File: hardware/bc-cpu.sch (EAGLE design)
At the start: 84 parts, among them J1 BATTERIES, J2 PHT, J3 LED Matrix, J5 BRK5, U1 R-735.0P, U2 MAX11632EEG+, U3 MAX11632EEG+, U4 AD1584BRTZ

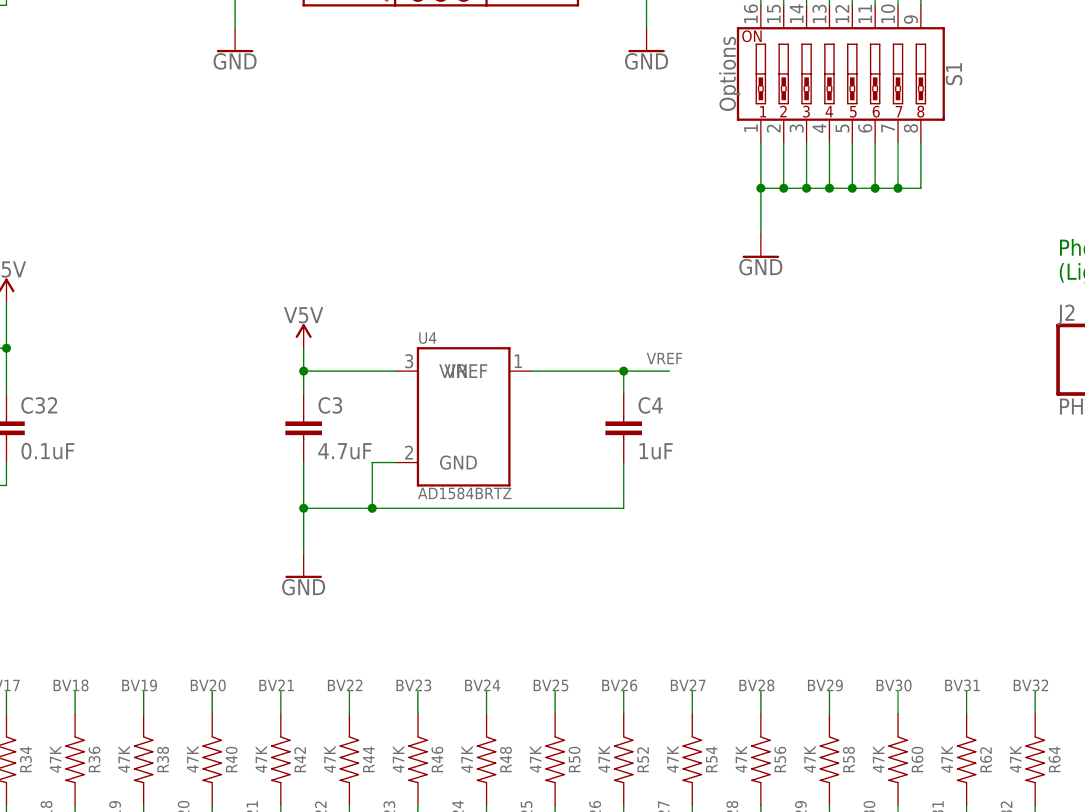
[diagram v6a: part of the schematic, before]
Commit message: All routed, DRC checks passing
Also removed drill holes from Arduino Nano lib -- they were translating
into the board for no reason. Replaced them with just silkscreen.
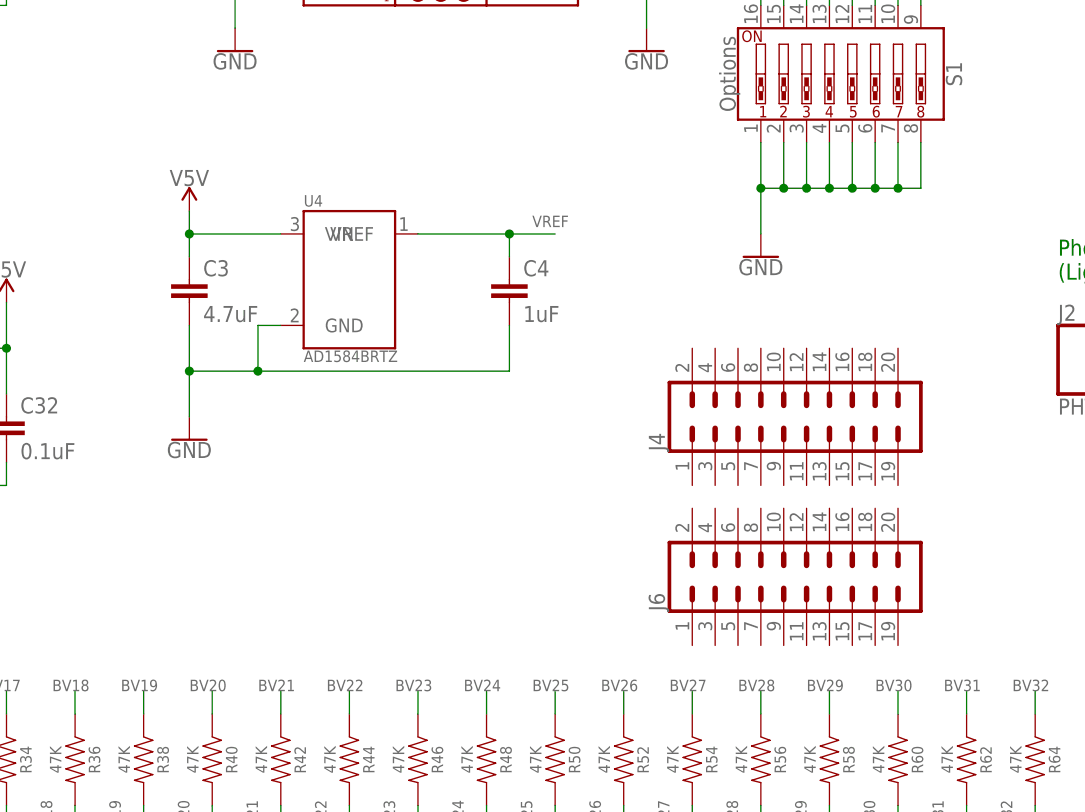
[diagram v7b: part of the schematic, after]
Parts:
- added J4, J6: (no value), SparkFun-Connectors:CONN_10X2NOSILK
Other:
- moved on the sheet: C3, C4, U4
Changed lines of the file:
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@@
 <part name="POWER" library="SparkFun-Connectors" deviceset="CONN_02" device="" value="12V"/>
 <part name="J5" library="SparkFun-Connectors" deviceset="CONN_02" device="" value="BRK5"/>
+<part name="J4" library="SparkFun-Connectors" deviceset="CONN_10X2" device="NOSILK"/>
+<part name="J6" library="SparkFun-Connectors" deviceset="CONN_10X2" device="NOSILK"/>
 </parts>
 <sheets>
@@
 <instance part="R63" gate="G$1" x="243.84" y="33.02" rot="R270"/>
 <instance part="R64" gate="G$1" x="243.84" y="48.26" rot="R270"/>
-<instance part="U4" gate="U1" x="180.34" y="86.36"/>
-<instance part="C3" gate="G$1" x="162.56" y="86.36"/>
-<instance part="C4" gate="G$1" x="198.12" y="86.36"/>
-<instance part="V5V1" gate="G$2" x="162.56" y="93.98"/>
-<instance part="GND3" gate="1" x="162.56" y="68.58"/>
+<instance part="U4" gate="U1" x="167.64" y="101.6"/>
+<instance part="C3" gate="G$1" x="149.86" y="101.6"/>
+<instance part="C4" gate="G$1" x="185.42" y="101.6"/>
+<instance part="V5V1" gate="G$2" x="149.86" y="109.22"/>
+<instance part="GND3" gate="1" x="149.86" y="83.82"/>
 <instance part="V5V2" gate="G$2" x="129.54" y="99.06"/>
 <instance part="V5V3" gate="G$2" x="129.54" y="152.4"/>
@@
 <instance part="POWER" gate="G$1" x="7.62" y="157.48"/>
 <instance part="J5" gate="G$1" x="50.8" y="162.56"/>
+<instance part="J4" gate="G$1" x="215.9" y="86.36" rot="R90"/>
+<instance part="J6" gate="G$1" x="215.9" y="68.58" rot="R90"/>
 </instances>
 <busses>
@@
 <segment>
 <pinref part="C3" gate="G$1" pin="2"/>
-<wire x1="162.56" y1="81.28" x2="162.56" y2="76.2" width="0.1524" layer="91"/>
+<wire x1="149.86" y1="96.52" x2="149.86" y2="91.44" width="0.1524" layer="91"/>
 <pinref part="GND3" gate="1" pin="GND"/>
 <pinref part="C4" gate="G$1" pin="2"/>
-<wire x1="162.56" y1="76.2" x2="162.56" y2="71.12" width="0.1524" layer="91"/>
-<wire x1="198.12" y1="81.28" x2="198.12" y2="76.2" width="0.1524" layer="91"/>
-<wire x1="198.12" y1="76.2" x2="170.18" y2="76.2" width="0.1524" layer="91"/>
-<junction x="162.56" y="76.2"/>
+<wire x1="149.86" y1="91.44" x2="149.86" y2="86.36" width="0.1524" layer="91"/>
+<wire x1="185.42" y1="96.52" x2="185.42" y2="91.44" width="0.1524" layer="91"/>
+<wire x1="185.42" y1="91.44" x2="157.48" y2="91.44" width="0.1524" layer="91"/>
+<junction x="149.86" y="91.44"/>
 <pinref part="U4" gate="U1" pin="GND"/>
-<wire x1="170.18" y1="76.2" x2="162.56" y2="76.2" width="0.1524" layer="91"/>
-<wire x1="172.72" y1="81.28" x2="170.18" y2="81.28" width="0.1524" layer="91"/>
-<wire x1="170.18" y1="81.28" x2="170.18" y2="76.2" width="0.1524" layer="91"/>
-<junction x="170.18" y="76.2"/>
+<wire x1="157.48" y1="91.44" x2="149.86" y2="91.44" width="0.1524" layer="91"/>
+<wire x1="160.02" y1="96.52" x2="157.48" y2="96.52" width="0.1524" layer="91"/>
+<wire x1="157.48" y1="96.52" x2="157.48" y2="91.44" width="0.1524" layer="91"/>
+<junction x="157.48" y="91.44"/>
 </segment>
 <segment>
@@
 <segment>
 <pinref part="U4" gate="U1" pin="VIN"/>
-<wire x1="172.72" y1="91.44" x2="162.56" y2="91.44" width="0.1524" layer="91"/>
+<wire x1="160.02" y1="106.68" x2="149.86" y2="106.68" width="0.1524" layer="91"/>
 <pinref part="C3" gate="G$1" pin="1"/>
-<wire x1="162.56" y1="91.44" x2="162.56" y2="88.9" width="0.1524" layer="91"/>
+<wire x1="149.86" y1="106.68" x2="149.86" y2="104.14" width="0.1524" layer="91"/>
 <pinref part="V5V1" gate="G$2" pin="VCC_1"/>
-<wire x1="162.56" y1="91.44" x2="162.56" y2="93.98" width="0.1524" layer="91"/>
-<junction x="162.56" y="91.44"/>
+<wire x1="149.86" y1="106.68" x2="149.86" y2="109.22" width="0.1524" layer="91"/>
+<junction x="149.86" y="106.68"/>
 </segment>
 <segment>
@@
 <segment>
 <pinref part="U4" gate="U1" pin="VREF"/>
-<wire x1="187.96" y1="91.44" x2="198.12" y2="91.44" width="0.1524" layer="91"/>
+<wire x1="175.26" y1="106.68" x2="185.42" y2="106.68" width="0.1524" layer="91"/>
 <pinref part="C4" gate="G$1" pin="1"/>
-<wire x1="198.12" y1="91.44" x2="198.12" y2="88.9" width="0.1524" layer="91"/>
-<wire x1="198.12" y1="91.44" x2="203.2" y2="91.44" width="0.1524" layer="91"/>
-<junction x="198.12" y="91.44"/>
-<label x="200.66" y="92.202" size="1.27" layer="95"/>
-</segment>
-<segment>
+<wire x1="185.42" y1="106.68" x2="185.42" y2="104.14" width="0.1524" layer="91"/>
+<wire x1="185.42" y1="106.68" x2="190.5" y2="106.68" width="0.1524" layer="91"/>
+<junction x="185.42" y="106.68"/>
+<label x="187.96" y="107.442" size="1.27" layer="95"/>
+</segment>
+<segment>

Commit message: Text, labels, positioning
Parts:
- J2: value PHT -> PHOTO
- J3: value LED Matrix -> LED MATRIX
- R65: value (none) -> 10K
- S1: value Options -> OPTIONS
- renumbered ARDUINO_NANO to ARDUINO
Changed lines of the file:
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@@
 <part name="U3" library="MAX-11632" deviceset="MAX-11632" device="QSOP24" value="MAX11632EEG+"/>
 <part name="J1" library="SparkFun-Connectors" deviceset="CONN_20X2" device="SHROUDED" value="BATTERIES"/>
-<part name="ARDUINO_NANO" library="ArduinoNanoV30" deviceset="ARDUINO_NANO" device=""/>
+<part name="ARDUINO" library="ArduinoNanoV30" deviceset="ARDUINO_NANO" device=""/>
 <part name="R1" library="SparkFun-Resistors" deviceset="RESISTOR" device="1206" value="1.5K"/>
 <part name="R2" library="SparkFun-Resistors" deviceset="RESISTOR" device="1206" value="47K"/>
@@
 <part name="GND8" library="SparkFun-PowerSymbols" deviceset="GND" device=""/>
 <part name="V5V4" library="SparkFun-PowerSymbols" deviceset="VCC_1" device="" value="V5V"/>
-<part name="J3" library="SparkFun-Connectors" deviceset="CONN_05X2" device="SHD" value="LED Matrix"/>
-<part name="S1" library="SparkFun-Switches" deviceset="DIP-08" device="-PTH" value="Options"/>
+<part name="J3" library="SparkFun-Connectors" deviceset="CONN_05X2" device="SHD" value="LED MATRIX"/>
+<part name="S1" library="SparkFun-Switches" deviceset="DIP-08" device="-PTH" value="OPTIONS"/>
 <part name="GND9" library="SparkFun-PowerSymbols" deviceset="GND" device=""/>
-<part name="R65" library="SparkFun-Resistors" deviceset="RESISTOR" device="AXIAL-0.3" value=" "/>
+<part name="R65" library="SparkFun-Resistors" deviceset="RESISTOR" device="AXIAL-0.3" value="10K"/>
 <part name="GND10" library="SparkFun-PowerSymbols" deviceset="GND" device=""/>
-<part name="J2" library="SparkFun-Connectors" deviceset="CONN_02" device="" value="PHT"/>
+<part name="J2" library="SparkFun-Connectors" deviceset="CONN_02" device="" value="PHOTO"/>
 <part name="POWER" library="SparkFun-Connectors" deviceset="CONN_02" device="" value="12V"/>
 <part name="J5" library="SparkFun-Connectors" deviceset="CONN_02" device="" value="BRK5"/>
@@
 <instance part="U3" gate="U1" x="96.52" y="99.06"/>
 <instance part="J1" gate="G$1" x="20.32" y="93.98"/>
-<instance part="ARDUINO_NANO" gate="G$1" x="177.8" y="157.48" rot="R180"/>
+<instance part="ARDUINO" gate="G$1" x="177.8" y="157.48" rot="R180"/>
 <instance part="R1" gate="G$1" x="7.62" y="33.02" rot="R270"/>
 <instance part="R2" gate="G$1" x="7.62" y="48.26" rot="R270"/>
@@
 </segment>
 <segment>
-<pinref part="ARDUINO_NANO" gate="G$1" pin="GND@2"/>
+<pinref part="ARDUINO" gate="G$1" pin="GND@2"/>
 <wire x1="157.48" y1="137.16" x2="154.94" y2="137.16" width="0.1524" layer="91"/>
 <pinref part="GND6" gate="1" pin="GND"/>
@@
 </segment>
 <segment>
-<pinref part="ARDUINO_NANO" gate="G$1" pin="GND@1"/>
+<pinref part="ARDUINO" gate="G$1" pin="GND@1"/>
 <wire x1="198.12" y1="142.24" x2="200.66" y2="142.24" width="0.1524" layer="91"/>
 <pinref part="GND4" gate="1" pin="GND"/>
@@
 </segment>
 <segment>
-<pinref part="ARDUINO_NANO" gate="G$1" pin="5V"/>
+<pinref part="ARDUINO" gate="G$1" pin="5V"/>
 <wire x1="157.48" y1="142.24" x2="144.78" y2="142.24" width="0.1524" layer="91"/>
 <pinref part="V5V4" gate="G$2" pin="VCC_1"/>
@@
 </segment>
 <segment>
-<pinref part="ARDUINO_NANO" gate="G$1" pin="SCK/D13"/>
+<pinref part="ARDUINO" gate="G$1" pin="SCK/D13"/>
 <wire x1="157.48" y1="170.18" x2="149.86" y2="170.18" width="0.1524" layer="91"/>
 <label x="149.86" y="170.18" size="1.778" layer="95"/>
@@
 </segment>
 <segment>
-<pinref part="ARDUINO_NANO" gate="G$1" pin="D11/MOSI"/>
+<pinref part="ARDUINO" gate="G$1" pin="D11/MOSI"/>
 <wire x1="198.12" y1="167.64" x2="205.74" y2="167.64" width="0.1524" layer="91"/>
 <label x="203.2" y="167.64" size="1.778" layer="95"/>
@@
 </segment>
 <segment>
-<pinref part="ARDUINO_NANO" gate="G$1" pin="D12/MISO"/>
+<pinref part="ARDUINO" gate="G$1" pin="D12/MISO"/>
 <wire x1="198.12" y1="170.18" x2="205.74" y2="170.18" width="0.1524" layer="91"/>
 <label x="203.2" y="170.18" size="1.778" layer="95"/>
@@
 </segment>
 <segment>
-<pinref part="ARDUINO_NANO" gate="G$1" pin="D10/OC1B/!SS"/>
+<pinref part="ARDUINO" gate="G$1" pin="D10/OC1B/!SS"/>
 <wire x1="198.12" y1="165.1" x2="205.74" y2="165.1" width="0.1524" layer="91"/>
 <label x="203.2" y="165.1" size="1.778" layer="95"/>
@@
 </segment>
 <segment>
-<pinref part="ARDUINO_NANO" gate="G$1" pin="D9/OC1A"/>
+<pinref part="ARDUINO" gate="G$1" pin="D9/OC1A"/>
 <wire x1="198.12" y1="162.56" x2="205.74" y2="162.56" width="0.1524" layer="91"/>
 <label x="203.2" y="162.56" size="1.778" layer="95"/>
@@
 </segment>
 <segment>
-<pinref part="ARDUINO_NANO" gate="G$1" pin="ADC5/SCL/A5"/>
+<pinref part="ARDUINO" gate="G$1" pin="ADC5/SCL/A5"/>
 <wire x1="157.48" y1="149.86" x2="149.86" y2="149.86" width="0.1524" layer="91"/>
 <label x="149.86" y="149.86" size="1.778" layer="95"/>
@@
 </segment>
 <segment>
-<pinref part="ARDUINO_NANO" gate="G$1" pin="ADC4/SDA/A4"/>
+<pinref part="ARDUINO" gate="G$1" pin="ADC4/SDA/A4"/>
 <wire x1="157.48" y1="152.4" x2="149.86" y2="152.4" width="0.1524" layer="91"/>
 <label x="149.86" y="152.4" size="1.778" layer="95"/>
@@
 <net name="DIP1" class="0">
 <segment>
-<pinref part="ARDUINO_NANO" gate="G$1" pin="D2/INT0"/>
+<pinref part="ARDUINO" gate="G$1" pin="D2/INT0"/>
 <wire x1="198.12" y1="144.78" x2="205.74" y2="144.78" width="0.1524" layer="91"/>
 <wire x1="205.74" y1="144.78" x2="213.36" y2="137.16" width="0.1524" layer="91"/>
@@
 <net name="DIP2" class="0">
 <segment>
-<pinref part="ARDUINO_NANO" gate="G$1" pin="D3/INT1"/>
+<pinref part="ARDUINO" gate="G$1" pin="D3/INT1"/>
 <wire x1="198.12" y1="147.32" x2="205.74" y2="147.32" width="0.1524" layer="91"/>
 <wire x1="205.74" y1="147.32" x2="215.9" y2="137.16" width="0.1524" layer="91"/>
@@
 <net name="DIP3" class="0">
 <segment>
-<pinref part="ARDUINO_NANO" gate="G$1" pin="D4/T0"/>
+<pinref part="ARDUINO" gate="G$1" pin="D4/T0"/>
 <wire x1="198.12" y1="149.86" x2="205.74" y2="149.86" width="0.1524" layer="91"/>
 <wire x1="205.74" y1="149.86" x2="218.44" y2="137.16" width="0.1524" layer="91"/>
@@
 <net name="DIP4" class="0">
 <segment>
-<pinref part="ARDUINO_NANO" gate="G$1" pin="D5/T1"/>
+<pinref part="ARDUINO" gate="G$1" pin="D5/T1"/>
 <wire x1="198.12" y1="152.4" x2="205.74" y2="152.4" width="0.1524" layer="91"/>
 <wire x1="205.74" y1="152.4" x2="220.98" y2="137.16" width="0.1524" layer="91"/>
@@
 <net name="DIP5" class="0">
 <segment>
-<pinref part="ARDUINO_NANO" gate="G$1" pin="D6/AIN0"/>
+<pinref part="ARDUINO" gate="G$1" pin="D6/AIN0"/>
 <wire x1="198.12" y1="154.94" x2="205.74" y2="154.94" width="0.1524" layer="91"/>
 <wire x1="205.74" y1="154.94" x2="223.52" y2="137.16" width="0.1524" layer="91"/>
@@
 <net name="DIP6" class="0">
 <segment>
-<pinref part="ARDUINO_NANO" gate="G$1" pin="D7/AIN1"/>
+<pinref part="ARDUINO" gate="G$1" pin="D7/AIN1"/>
 <wire x1="198.12" y1="157.48" x2="205.74" y2="157.48" width="0.1524" layer="91"/>
 <wire x1="205.74" y1="157.48" x2="226.06" y2="137.16" width="0.1524" layer="91"/>
@@
 <net name="DIP7" class="0">
 <segment>
-<pinref part="ARDUINO_NANO" gate="G$1" pin="D8/CLK0"/>
+<pinref part="ARDUINO" gate="G$1" pin="D8/CLK0"/>
 <wire x1="198.12" y1="160.02" x2="205.74" y2="160.02" width="0.1524" layer="91"/>
 <wire x1="205.74" y1="160.02" x2="228.6" y2="137.16" width="0.1524" layer="91"/>
@@
 </segment>
 <segment>
-<pinref part="ARDUINO_NANO" gate="G$1" pin="ADC0/A0"/>
+<pinref part="ARDUINO" gate="G$1" pin="ADC0/A0"/>
 <wire x1="157.48" y1="162.56" x2="149.86" y2="162.56" width="0.1524" layer="91"/>
 <label x="149.86" y="162.56" size="1.778" layer="95"/>
@@
 </segment>
 <segment>
-<pinref part="ARDUINO_NANO" gate="G$1" pin="ADC1/A1"/>
+<pinref part="ARDUINO" gate="G$1" pin="ADC1/A1"/>
 <wire x1="157.48" y1="160.02" x2="149.86" y2="160.02" width="0.1524" layer="91"/>
 <label x="149.86" y="160.02" size="1.778" layer="95"/>
@@
 <net name="DIP8" class="0">
 <segment>
-<pinref part="ARDUINO_NANO" gate="G$1" pin="ADC7/A7"/>
+<pinref part="ARDUINO" gate="G$1" pin="ADC7/A7"/>
 <wire x1="157.48" y1="144.78" x2="149.86" y2="144.78" width="0.1524" layer="91"/>
 <label x="149.86" y="144.78" size="1.778" layer="95"/>
